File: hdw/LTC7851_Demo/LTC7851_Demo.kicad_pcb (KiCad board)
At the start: 4 copper layers, 100 x 50 mm, 211 parts, among them J1101 FG_LOAD, J1102 ISNS, J1401 VOUT, J1402 LOOP_TAP, J1403 Wave_Gen_In, J201 +12V IN, J206 GND IN, J301 CLKOUT, J302 RUN, J303 SMOD, J304 IAVG, J901 +5V OUT, J902 +5V OUT, J903 GND OUT, J904 GND OUT, Q1101 BSC123N10LSGATMA1, Q1102 BSC123N10LSGATMA1, Q1201 BSC123N10LSGATMA1, Q1202 BSC123N10LSGATMA1, Q1301 BSC123N10LSGATMA1, Q1302 BSC123N10LSGATMA1, Q201 BSC123N10LSGATMA1, Q202 BSC123N10LSGATMA1, T1401 1:1 Pulse Transformer, U1101 LT1010DD, U201 LTC4365DDB, U202 74LVC1G06, U301 LTC7851UHH, U302 74LVC1G17, U303 74LVC1G06, U304 74LVC1G06, U401 SiC779, U501 SiC779, U601 SiC779, U701 SiC779, U801 LM1117-ADJ

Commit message: More routing
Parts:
- moved C715 3.35 mm to (119.2, 101.7), turned to 90 degrees
- moved C515 3.32 mm to (153.7, 101.7), turned to 90 degrees
- moved C615 3.32 mm to (136.5, 101.7), turned to 90 degrees
- moved C420 3.32 mm to (171.0, 101.7), turned to 90 degrees
- moved C415 2.84 mm to (121.5, 97.6)
- moved C510 2.84 mm to (138.7, 97.6)
- moved C610 2.84 mm to (156.1, 97.6)
- moved C710 2.84 mm to (173.4, 97.6)
- moved R407 2.13 mm to (119.2, 97.4)
- moved R503 2.13 mm to (136.5, 97.4)
- moved R603 2.13 mm to (153.8, 97.4)
- moved R703 2.13 mm to (171.2, 97.4)
- moved C707 0.39 mm to (126.4, 109.1)
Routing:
- net GND: track 0.00 -> 18.5 mm
- net POS5_RUN: track 0.00 -> 6.57 mm
- net Net-(L501-Pad1): track 0.00 -> 3.51 mm
- net Net-(C508-Pad2): track 0.00 -> 2.19 mm
- net Net-(R502-Pad1): track 0.00 -> 2.19 mm
- net Net-(C413-Pad2): track 0.00 -> 2.19 mm
- net Net-(R406-Pad1): track 0.00 -> 2.19 mm
- net Net-(C608-Pad2): track 0.00 -> 2.19 mm
- net Net-(C708-Pad2): track 0.00 -> 2.19 mm
- net Net-(R602-Pad1): track 0.00 -> 2.19 mm
- net Net-(R702-Pad1): track 0.00 -> 2.19 mm
- net Net-(R306-Pad2): track 0.00 -> 1.72 mm
- net Net-(R308-Pad2): track 0.00 -> 1.69 mm
- net Net-(C708-Pad1): track 0.00 -> 1.65 mm
- net Net-(C608-Pad1): track 0.00 -> 1.65 mm
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- added copper zone on F.Cu, net +5V
- added copper zone on F.Cu, net Net-(L401-Pad1)
- added copper zone on F.Cu, net Net-(L501-Pad1)
- added copper zone on F.Cu, net Net-(L601-Pad1)
- added copper zone on F.Cu, net Net-(L701-Pad1)
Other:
- net class Default: via_dia 0.8 -> 0.45; via_drill 0.4 -> 0.2
- net class Power: via_dia 0.8 -> 0.45; via_drill 0.4 -> 0.2
- net class Signal: via_dia 0.8 -> 0.45; via_drill 0.4 -> 0.2

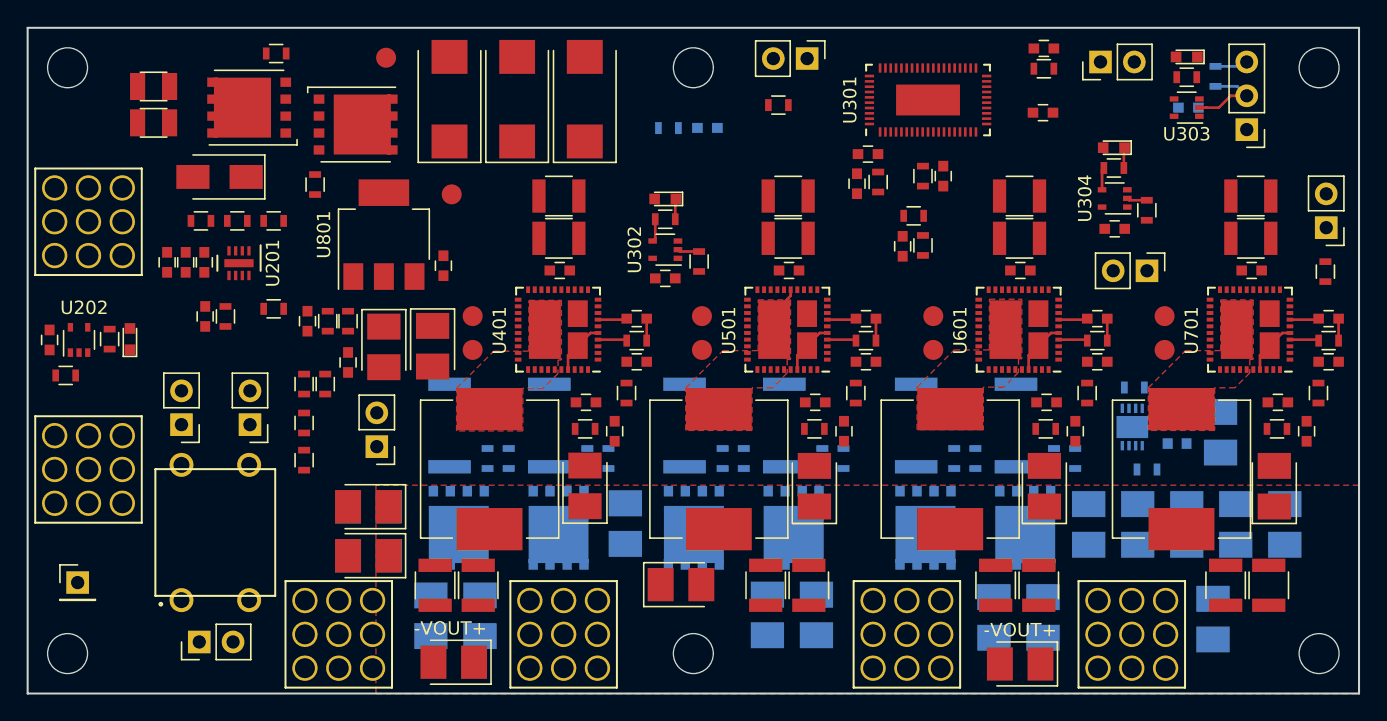
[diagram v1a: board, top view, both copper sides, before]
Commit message: A lot more power flooding
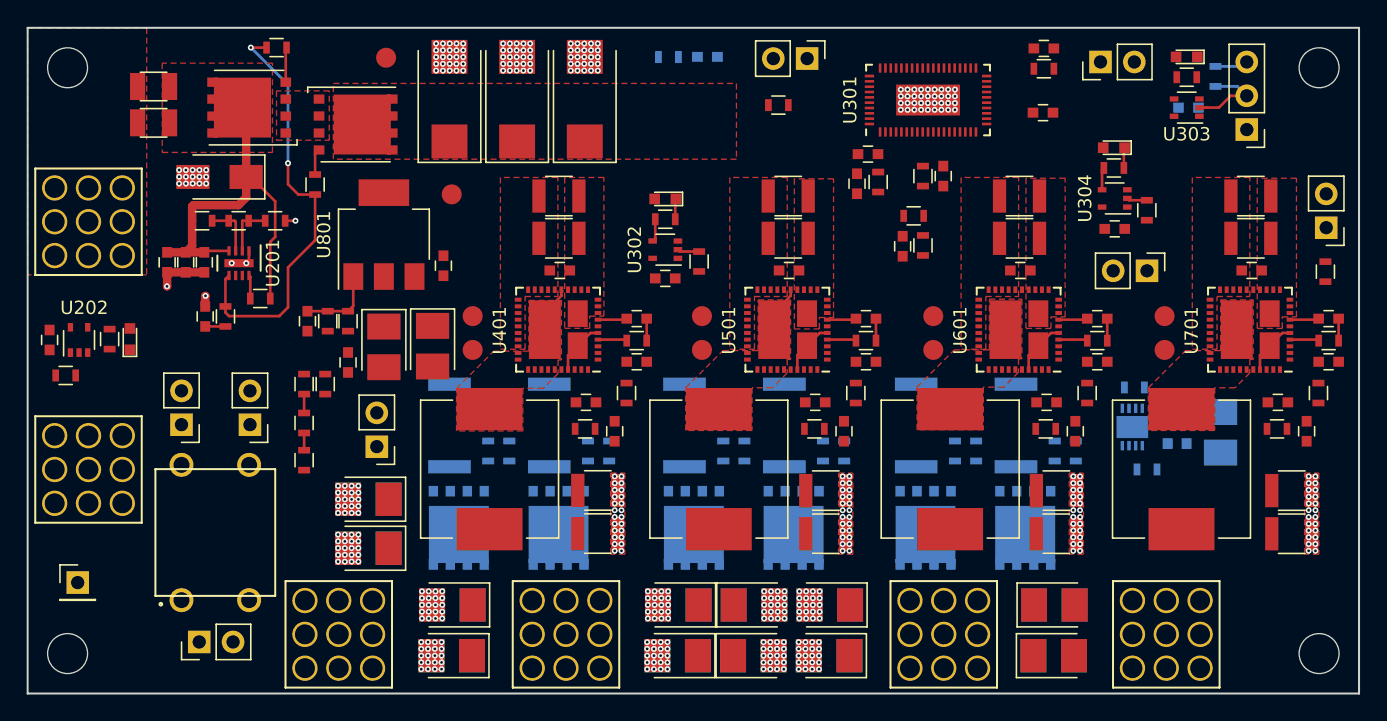
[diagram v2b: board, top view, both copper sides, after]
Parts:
- removed MH1002, MH1005: MountingHole, Mounting_Holes:MountingHole_3mm
- C405, C501, C502, C503, C601, C602, C701: moved to F.Cu
- C420, C515, C615, C715: moved to B.Cu
- moved C420 63.1 mm to (109.2, 114.5), turned to 180 degrees
- moved C605 37.5 mm to (131.9, 114.5), turned to 0 degrees
- moved C603 35.6 mm to (137.6, 114.5), turned to 180 degrees
- moved C701 29.0 mm to (137.6, 114.5), turned to 180 degrees
- moved J901 28.5 mm to (146.2, 112.9), turned to 180 degrees
- moved J903 25.6 mm to (117.8, 112.9), turned to 180 degrees
- moved C501 23.7 mm to (109.3, 110.6), turned to 180 degrees
- moved C505 21.7 mm to (131.9, 110.6), turned to 0 degrees
- moved C507 20.4 mm to (137.6, 110.6), turned to 180 degrees
- moved C615 20.1 mm to (154.5, 110.6), turned to 0 degrees
- moved C405 18.8 mm to (126.2, 114.5), turned to 180 degrees
- moved C503 18.0 mm to (131.9, 110.6), turned to 0 degrees
- moved C707 18.0 mm to (109.2, 114.5), turned to 180 degrees
- moved C607 17.4 mm to (126.2, 110.6)
- moved C702 15.0 mm to (137.6, 110.6)
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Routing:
- net Net-(R205-Pad1): track 0.00 -> 32.2 mm, vias 0 -> 2
- net +12Vin: track 0.00 -> 29.9 mm
- net GND: track 18.5 -> 25.0 mm, vias 0 -> 427
- net Net-(C803-Pad1): track 0.00 -> 5.81 mm
- net Net-(R201-Pad2): track 0.00 -> 3.99 mm
- net Net-(R202-Pad2): track 0.00 -> 3.97 mm
- net Net-(L401-Pad1): track 0.00 -> 3.51 mm
- net Net-(Q201-Pad4): track 0.00 -> 2.62 mm
- net Net-(Q202-Pad4): track 0.00 -> 1.97 mm
- net Net-(R204-Pad2): track 0.00 -> 1.77 mm
- net Net-(C205-Pad1): track 0.00 -> 1.52 mm
- net /POS5 Phase 1/POS5_VSNS1_+: track 0.00 -> 1.42 mm
- net LOOP_TAP: track 0.00 -> 1.29 mm
- added copper zone on F.Cu, net +12V
- added copper zone on F.Cu, net +12Vin
- added copper zone on F.Cu, net GND
- added copper zone on F.Cu, net Net-(F201-Pad2)
- added copper zone on F.Cu, net Net-(Q201-Pad1)
- removed copper zone on F.Cu, net +5V
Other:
- board text removed: "-VOUT+"

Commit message: revising power vias
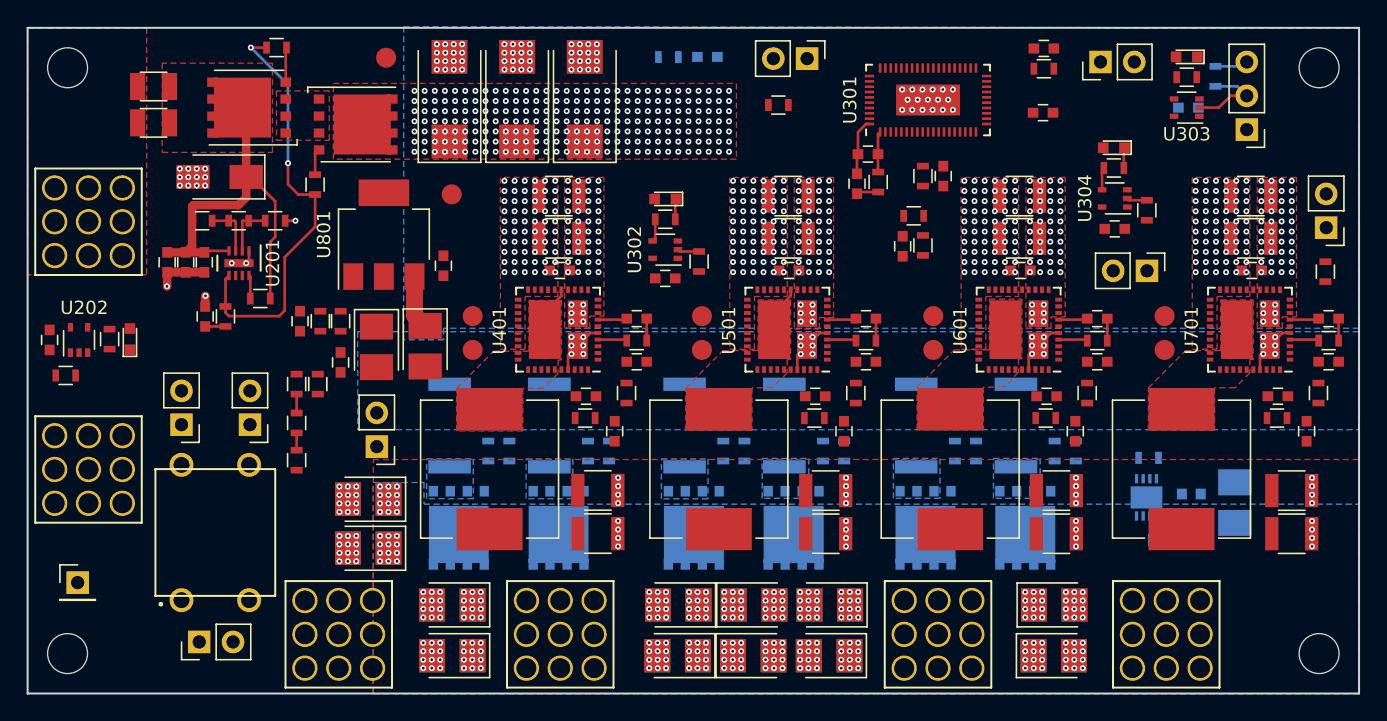
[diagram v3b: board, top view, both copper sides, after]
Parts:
- moved J901 28.8 mm to (117.4, 112.9), turned to 0 degrees
- moved J903 27.9 mm to (145.7, 112.9), turned to 0 degrees
- moved C1101 5.39 mm to (165.5, 103.1)
- moved C1102 5.39 mm to (164.1, 103.1)
- moved R1101 5.39 mm to (161.6, 99.6)
- moved U1101 5.39 mm to (161.4, 102.6)
- moved C1103 5.39 mm to (168.0, 103.0)
- moved R1102 5.39 mm to (162.5, 105.8)
- moved R407 0.81 mm to (119.2, 96.6)
- moved R503 0.81 mm to (136.5, 96.6)
- moved R603 0.81 mm to (153.8, 96.6)
- moved R703 0.81 mm to (171.2, 96.6)
- moved C804 0.56 mm to (100.9, 92.4)
- moved C805 0.56 mm to (103.6, 91.3)
- moved R409 0.56 mm to (97.6, 99.8)
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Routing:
- net Net-(C803-Pad1): track 5.81 -> 0.00 mm
- net Net-(C404-Pad2): track 0.00 -> 4.27 mm
- net +12V: track 0.00 -> 4.04 mm, vias 0 -> 408
- net POS5_COMP: track 0.00 -> 3.08 mm
- net Net-(C404-Pad1): track 0.00 -> 1.64 mm
- net GND: track 25.0 -> 24.0 mm, vias 427 -> 522
- net +5V: vias 0 -> 144
- added copper zone on B.Cu, net +12V
- added copper zone on B.Cu, net +5V
- added copper zone on F.Cu, net +5V
- added copper zone on B.Cu, net GND
- added copper zone on B.Cu, net Net-(J1102-Pad1)
- added copper zone on B.Cu, net Net-(Q1102-Pad1)
- added copper zone on B.Cu, net Net-(Q1201-Pad1)
- added copper zone on B.Cu, net Net-(Q1202-Pad1)
- added copper zone on B.Cu, net Net-(Q1301-Pad1)
- added copper zone on B.Cu, net Net-(Q1302-Pad1)

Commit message: Routed current sense and voltage sense
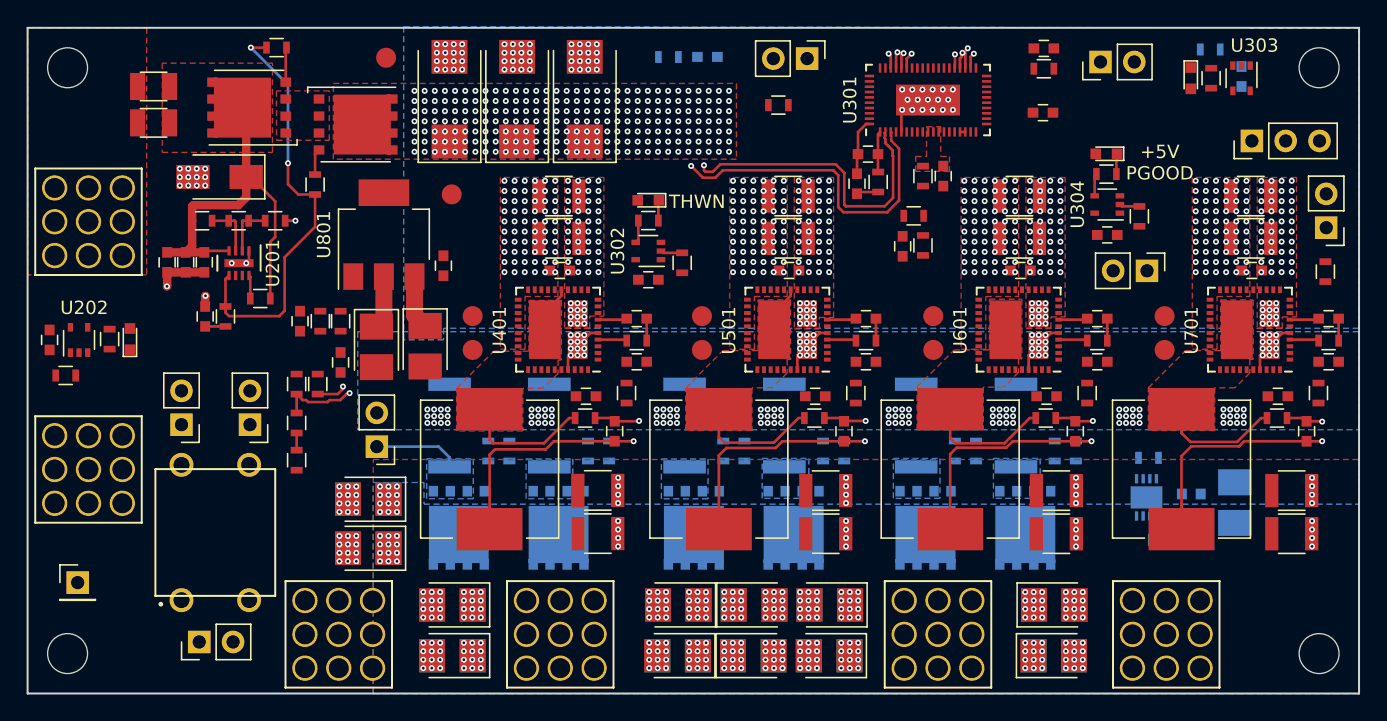
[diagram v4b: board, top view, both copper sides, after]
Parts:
- moved U303 4.67 mm to (168.5, 71.1), turned to 270 degrees
- moved C303 4.62 mm to (168.5, 71.0), turned to 90 degrees
- moved R310 2.06 mm to (166.2, 68.9), turned to 180 degrees
- moved R307 1.83 mm to (166.3, 71.1), turned to 270 degrees
- moved D302 1.63 mm to (164.7, 71.1), turned to 270 degrees
- moved D301 1.27 mm to (124.0, 80.3)
- moved R304 1.27 mm to (126.5, 85.0)
- moved R306 1.27 mm to (124.0, 81.8)
- moved U302 1.27 mm to (124.0, 84.1)
- moved C304 1.27 mm to (124.0, 86.2)
- moved J302 0.93 mm to (169.3, 75.8), turned to 90 degrees
- moved D303 0.72 mm to (158.4, 76.8)
- moved R308 0.72 mm to (158.4, 78.3)
- moved C305 0.72 mm to (158.5, 82.9)
- moved R305 0.72 mm to (160.9, 81.5)
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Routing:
- net +5V: track 0.00 -> 240.8 mm, vias 144 -> 152
- net /POS5 Phase 1/POS5_VSNS1_+: track 1.42 -> 70.0 mm, vias 0 -> 2
- net /POS5 Phase 1/POS5_VSNS1_-: track 0.00 -> 67.1 mm, vias 0 -> 2
- net /POS5 Phase 4/POS5_ISNS4_+: track 0.00 -> 50.2 mm, vias 0 -> 2
- net /POS5 Phase 1/POS5_ISNS1_+: track 0.00 -> 46.1 mm, vias 0 -> 2
- net /POS5 Phase 2/POS5_ISNS2_+: track 0.00 -> 41.2 mm, vias 0 -> 2
- net /POS5 Phase 3/POS5_ISNS3_+: track 0.00 -> 38.7 mm, vias 0 -> 2
- net Net-(L401-Pad1): track 3.51 -> 13.1 mm
- net Net-(L601-Pad1): track 0.00 -> 9.54 mm
- net Net-(L501-Pad1): track 3.51 -> 13.0 mm
- net Net-(L701-Pad1): track 0.00 -> 9.24 mm
- net POS5_RUN: track 6.57 -> 0.00 mm
- net Net-(J1102-Pad1): track 0.00 -> 6.50 mm
- net +5.5V_MNG: track 0.00 -> 3.99 mm
- net GND: track 24.0 -> 23.2 mm, vias 522 -> 642
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- added copper zone on F.Cu, net POS5_EXTVCC
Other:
- board text added: "+5V PGOOD"
- board text added: "THWN"

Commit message: Routed PWM
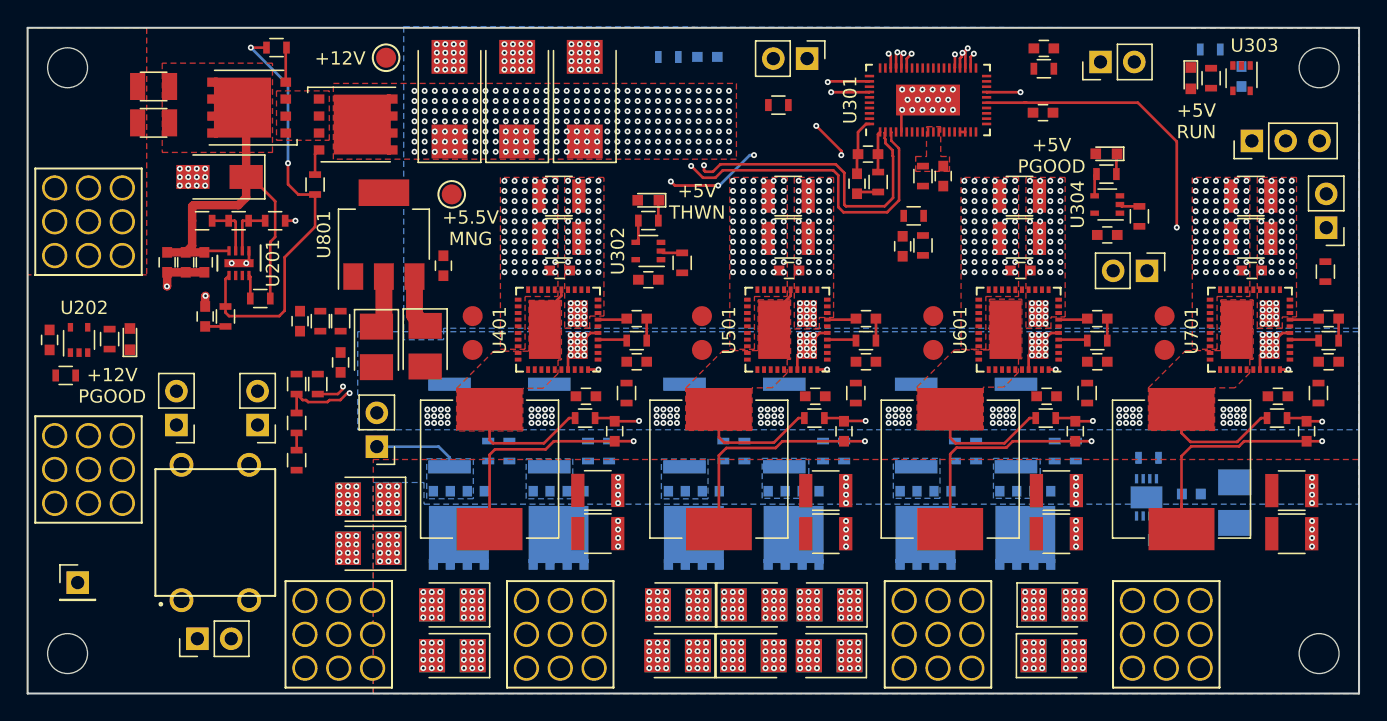
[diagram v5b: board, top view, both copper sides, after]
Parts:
- moved J1402 0.57 mm to (94.6, 97.1)
- moved J1401 0.38 mm to (88.5, 97.1)
- moved J1403 0.28 mm to (90.1, 113.2)
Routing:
- net Net-(U301-Pad24): track 0.00 -> 40.6 mm, vias 0 -> 2
- net Net-(U301-Pad52): track 0.00 -> 36.5 mm, vias 0 -> 5
- net Net-(U301-Pad26): track 0.00 -> 34.3 mm, vias 0 -> 2
- net Net-(U301-Pad50): track 0.00 -> 27.3 mm, vias 0 -> 4
- net /POS5 Phase 1/POS5_ISNS1_+: track 46.1 -> 44.0 mm
- net +5V: track 240.8 -> 238.8 mm
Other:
- board text added: "+12V"
- board text added: "+12V PGOOD"
- board text added: "+5.5V MNG"
- board text added: "+5V RUN"
- board text added: "+5V THWN"
- board text removed: "THWN"

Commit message: Routed some garbage near the controller
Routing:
- net POS5_SS: track 0.00 -> 25.5 mm, vias 0 -> 3
- net Net-(C302-Pad1): track 0.00 -> 21.1 mm, vias 0 -> 1
- net POS5_COMP: track 3.08 -> 19.9 mm, vias 0 -> 3
- net POS5_ILIM: track 0.00 -> 15.2 mm
- net POS5_IAVG: track 0.00 -> 9.35 mm
- net POS5_VOSNS: track 0.40 -> 8.62 mm, vias 0 -> 2
- net POS5_EXTVCC: track 0.00 -> 7.14 mm
- net POS5_RUN: track 0.00 -> 4.22 mm
- net GND: track 23.2 -> 24.1 mm, vias 642 -> 643
